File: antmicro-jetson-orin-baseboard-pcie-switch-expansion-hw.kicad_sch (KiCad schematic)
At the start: 0 parts

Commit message: [#100645] Update stackup & prepare mock
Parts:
- added A1: Mech_M2_2242_H2.5mm, antmicro-footprints:Mech_M2_2242_H2.5mm, symbol antmicroModules:Mech_M2_2242_H2.5mm
- added A2: Mech_M2_2280_H2.5mm, antmicro-footprints:Mech_M2_2280_H2.5mm, symbol antmicroModules:Mech_M2_2280_H2.5mm
- added H1, H2, H3, H4: Spacer_Drill3.7mm_H10mm_9774100151R, antmicro-footprints:Spacer_Drill3.7mm_H10mm_9774100151R, symbol antmicroMechanicalParts:Spacer_Drill3.7mm_H10mm_9774100151R
- added H5, H6, H7, H8: Spacer_Drill4.4mm_H2.5mm_9774025360R, antmicro-footprints:Spacer_Drill4.4mm_H2.5mm_9774025360R, symbol antmicroMechanicalParts:Spacer_Drill4.4mm_H2.5mm_9774025360R
- added J1, J2: Bus_M.2_1-2199230-6, antmicro-footprints:Bus_M.2_Socket_Key_M_TE_1-2199230-6, symbol antmicroPciConnectors:Bus_M.2_1-2199230-6
- added J3, J4, J5: OCuLink_x4_Amphenol_G14A421211112HR, antmicro-footprints:Amphenol_G14A421211112HR, symbol antmicroPciConnectors:OCuLink_x4_Amphenol_G14A421211112HR
- added J6: Molex_Nano-Fit_1x2_SMD_1054301202, antmicro-footprints:Conn_Molex_Nano-Fit_1x2_SMD_1054301202, symbol antmicroWire2BoardConnectors:Molex_Nano-Fit_1x2_SMD_1054301202
- added J7: Plug_Samtec_ERM8_2x40_ERM8-040-05.0-L-DV-K-TR, antmicro-footprints:Conn_Plug_Samtec_ERM8_2x40_ERM8-040-05.0-L-DV-K-TR, symbol antmicroB2BConnectors:Plug_Samtec_ERM8_2x40_ERM8-040-05.0-L-DV-K-TR
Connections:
- new net: J3.A11 (GND), J3.A14 (GND), J3.A17 (GND), J3.A2 (GND), J3.A20 (GND), J3.A5 (GND), J3.A8 (GND), J3.B11 (GND), J3.B14 (GND), J3.B17 (GND), J3.B2 (GND), J3.B20 (GND), J3.B5 (GND), J3.B8 (GND)
- new net: J3.A21 (5V), J3.B1 (5V)
- new net: J4.A11 (GND), J4.A14 (GND), J4.A17 (GND), J4.A2 (GND), J4.A20 (GND), J4.A5 (GND), J4.A8 (GND), J4.B11 (GND), J4.B14 (GND), J4.B17 (GND), J4.B2 (GND), J4.B20 (GND), J4.B5 (GND), J4.B8 (GND)
- new net: J4.A21 (5V), J4.B1 (5V)
- new net: J2.1 (GND), J2.15 (GND), J2.21 (GND), J2.27 (GND), J2.3 (GND), J2.33 (GND), J2.39 (GND), J2.45 (GND), J2.51 (GND), J2.57 (GND), J2.71 (GND), J2.73 (GND), J2.75 (GND), J2.9 (GND)
- new net: J2.12 (3V3), J2.14 (3V3), J2.16 (3V3), J2.18 (3V3), J2.2 (3V3), J2.4 (3V3), J2.70 (3V3), J2.72 (3V3), J2.74 (3V3)
- new net: J2.MP1 (MP), J2.MP2 (MP)
- new net: J1.1 (GND), J1.15 (GND), J1.21 (GND), J1.27 (GND), J1.3 (GND), J1.33 (GND), J1.39 (GND), J1.45 (GND), J1.51 (GND), J1.57 (GND), J1.71 (GND), J1.73 (GND), J1.75 (GND), J1.9 (GND)
- new net: J1.12 (3V3), J1.14 (3V3), J1.16 (3V3), J1.18 (3V3), J1.2 (3V3), J1.4 (3V3), J1.70 (3V3), J1.72 (3V3), J1.74 (3V3)
- new net: J1.MP1 (MP), J1.MP2 (MP)
- new net: J5.A11 (GND), J5.A14 (GND), J5.A17 (GND), J5.A2 (GND), J5.A20 (GND), J5.A5 (GND), J5.A8 (GND), J5.B11 (GND), J5.B14 (GND), J5.B17 (GND), J5.B2 (GND), J5.B20 (GND), J5.B5 (GND), J5.B8 (GND)
- new net: J5.A21 (5V), J5.B1 (5V)

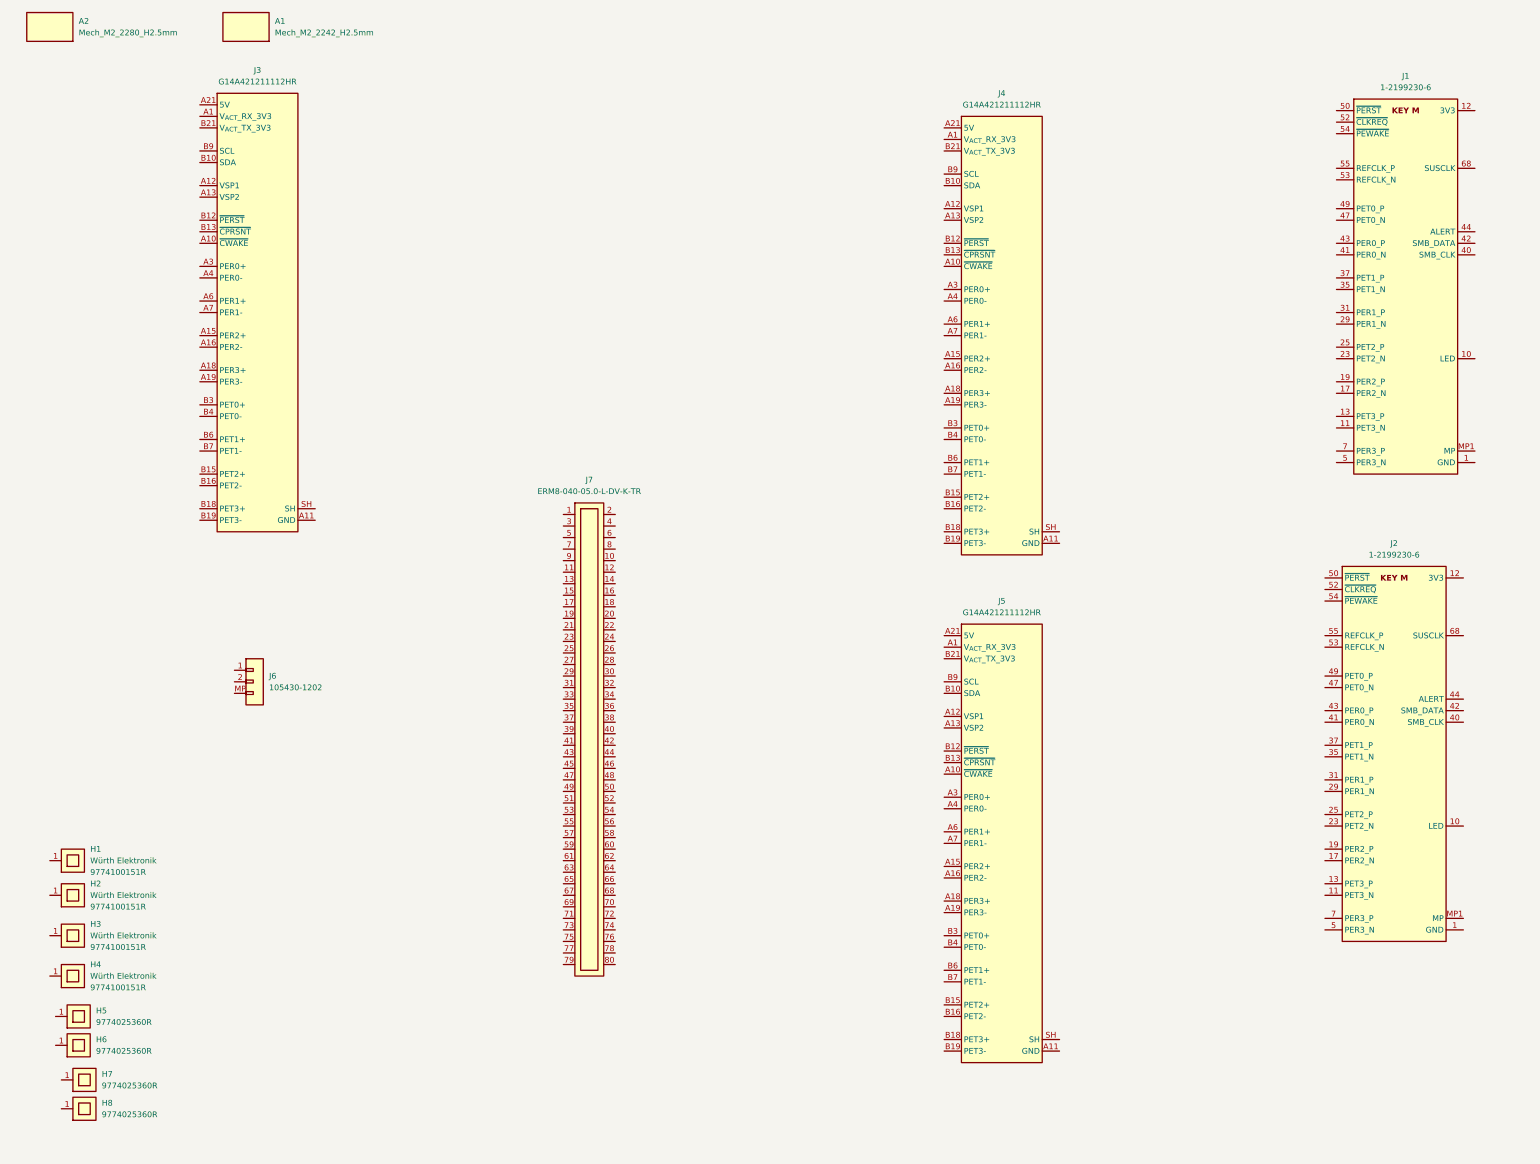
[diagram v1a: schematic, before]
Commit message: [#100765] Add subsheets, import bus alias definitions
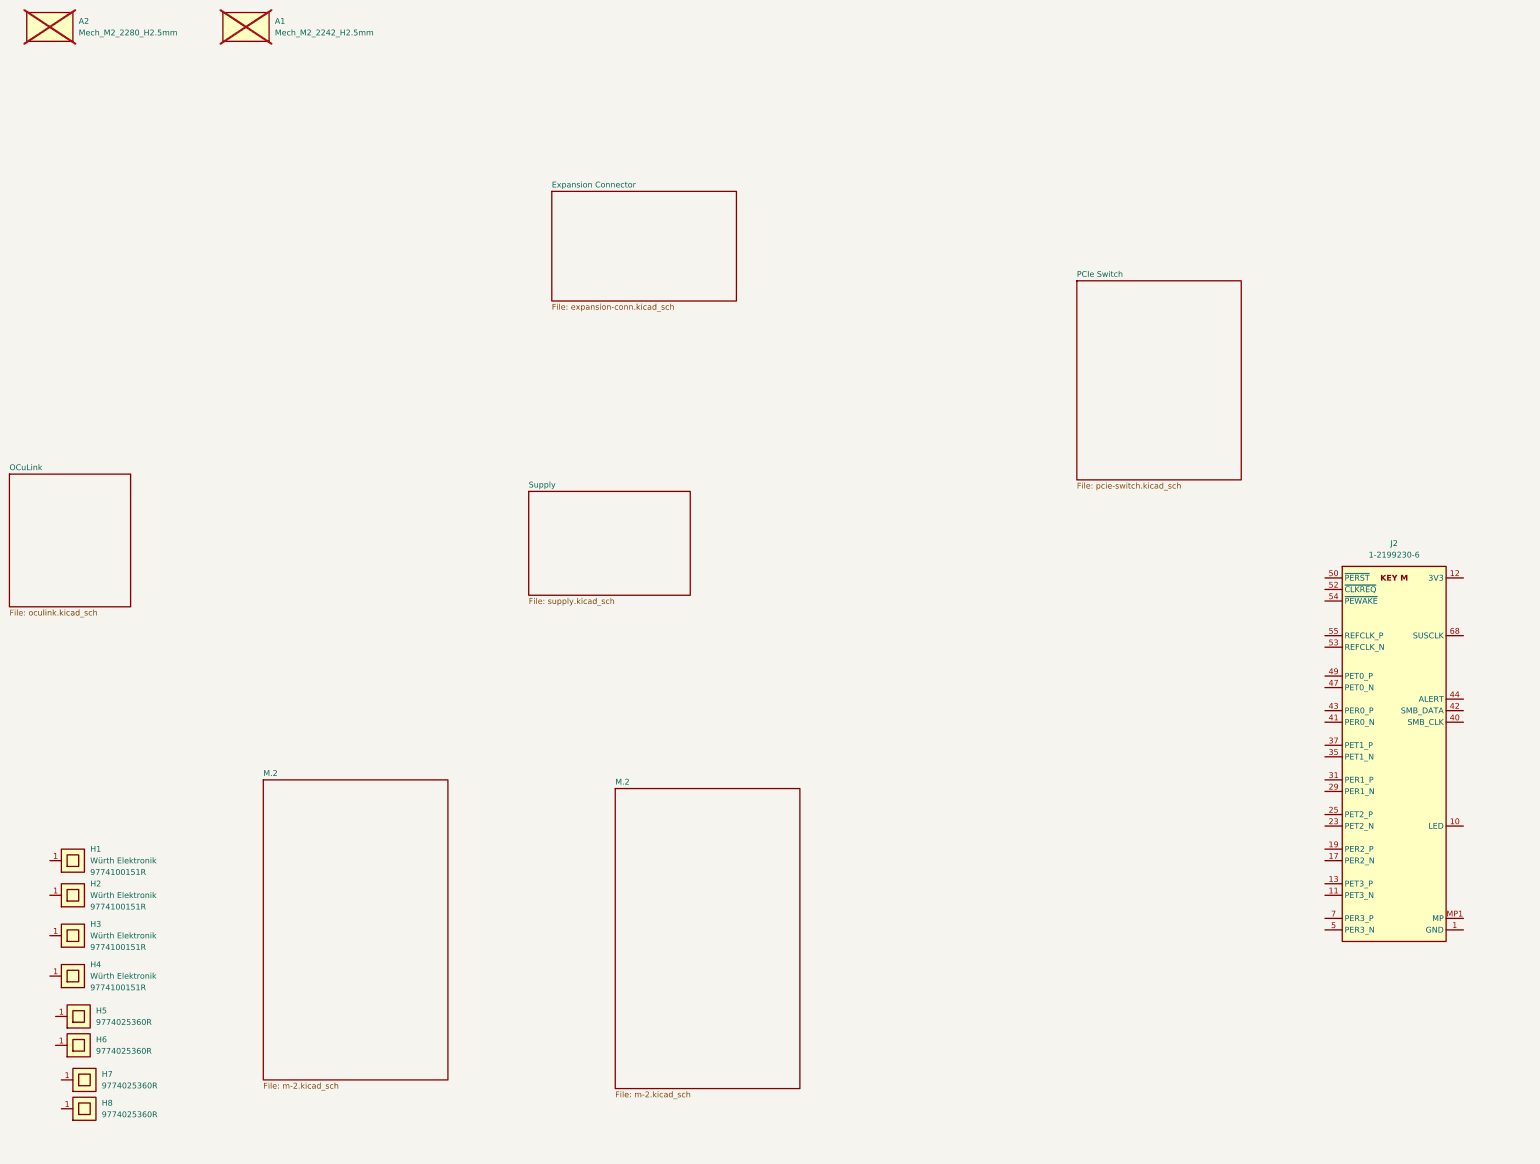
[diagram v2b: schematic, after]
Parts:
- removed J1: Bus_M.2_1-2199230-6, antmicro-footprints:Bus_M.2_Socket_Key_M_TE_1-2199230-6, symbol antmicroPciConnectors:Bus_M.2_1-2199230-6
- removed J3, J4, J5: OCuLink_x4_Amphenol_G14A421211112HR, antmicro-footprints:Amphenol_G14A421211112HR, symbol antmicroPciConnectors:OCuLink_x4_Amphenol_G14A421211112HR
- removed J6: Molex_Nano-Fit_1x2_SMD_1054301202, antmicro-footprints:Conn_Molex_Nano-Fit_1x2_SMD_1054301202, symbol antmicroWire2BoardConnectors:Molex_Nano-Fit_1x2_SMD_1054301202
- removed J7: Plug_Samtec_ERM8_2x40_ERM8-040-05.0-L-DV-K-TR, antmicro-footprints:Conn_Plug_Samtec_ERM8_2x40_ERM8-040-05.0-L-DV-K-TR, symbol antmicroB2BConnectors:Plug_Samtec_ERM8_2x40_ERM8-040-05.0-L-DV-K-TR
- A1, A2: now not fitted; now in the parts list
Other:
- added sheet Expansion Connector (expansion-conn.kicad_sch)
- added sheet M.2 (m-2.kicad_sch)
- added sheet OCuLink (oculink.kicad_sch)
- added sheet PCIe Switch (pcie-switch.kicad_sch)
- added sheet Supply (supply.kicad_sch)

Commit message: [#100765] Update Top Level schematic
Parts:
- removed J2: Bus_M.2_1-2199230-6, antmicro-footprints:Bus_M.2_Socket_Key_M_TE_1-2199230-6, symbol antmicroPciConnectors:Bus_M.2_1-2199230-6
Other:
- added sheet PCIe Mux (pcie-mux.kicad_sch)
- sheet Expansion Connector ports: added PCIe_{x2}{PCIe}, POWER_EN; removed none
- sheet M.2 ports: added PCIe_{x2}{PCIe}; removed none
- sheet OCuLink ports: added PCIe_{x2}{PCIe}; removed none
- sheet PCIe Switch ports: added PCIe_{x2_0}{PCIe}, PCIe_{x2_1}{PCIe}, PCIe_{x2}{PCIe}; removed none
- sheet Supply ports: added POWER_EN, V_{cc}; removed none

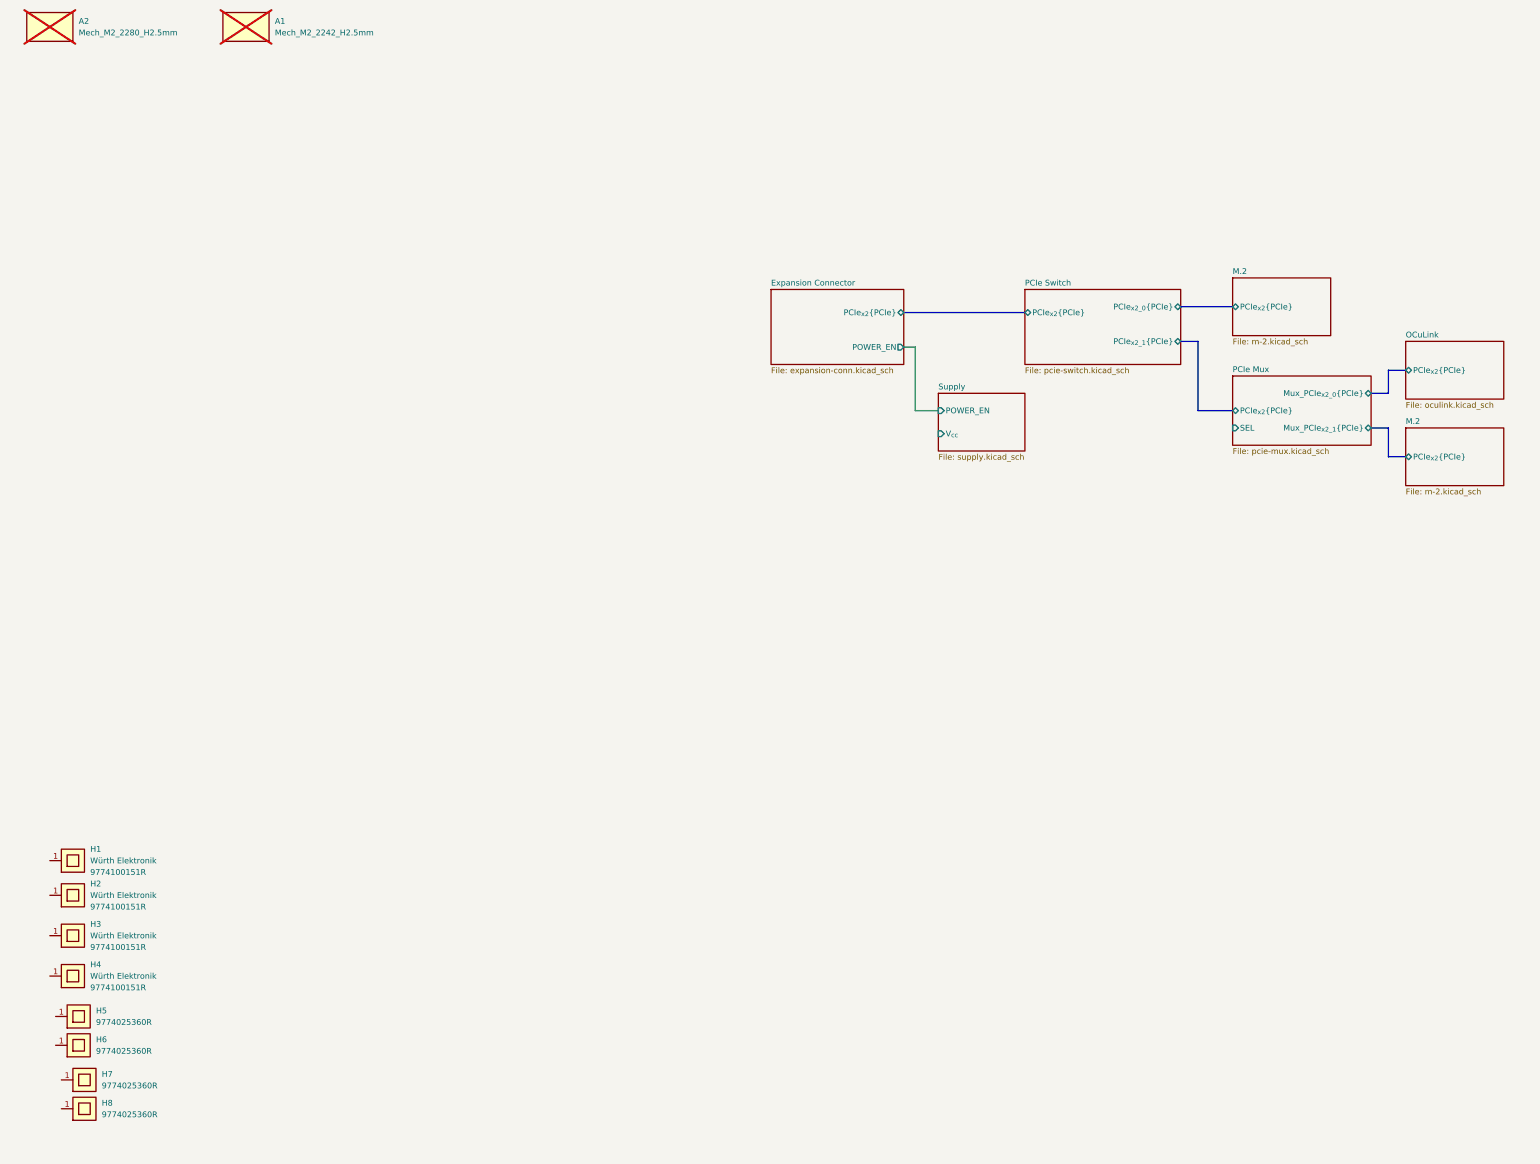
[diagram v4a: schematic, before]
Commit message: [#100765] Update top level schematic, add comments
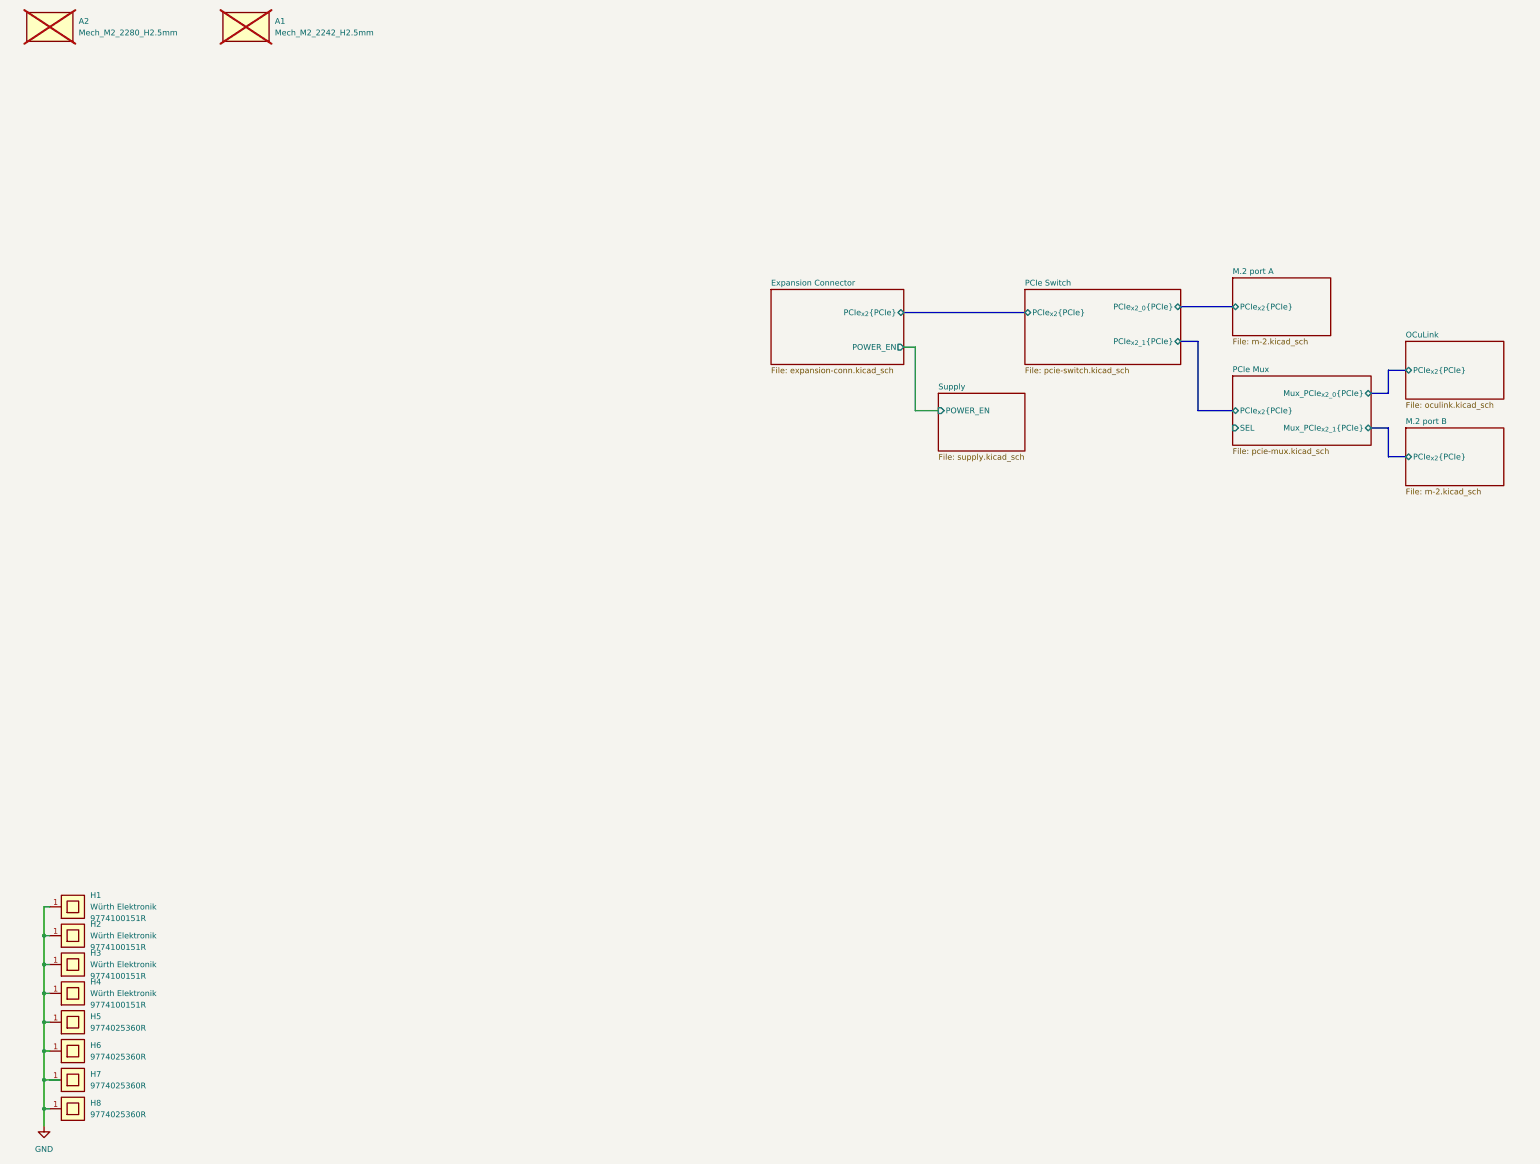
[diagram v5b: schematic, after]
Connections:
- net GND: now reaches H6.1
- net GND: now also H1.1, H2.1, H3.1, H4.1, H5.1, H7.1, H8.1
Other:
- sheet M.2 renamed M.2 port A
- added sheet M.2 port B (m-2.kicad_sch)
- sheet Supply ports: added none; removed V_{cc}
- moved on the sheet: H1, H2, H3, H4, H5, H6, H7, H8

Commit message: [#100765] Work on schematic
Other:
- added sheet Tag Connect, EEPROM (eeprom_tagconnect.kicad_sch)
- sheet PCIe Switch ports: added {I_{2}C}, {SPI}; removed none
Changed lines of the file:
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@@
 	(wire
 		(pts
-			(xy 232.41 113.03) (xy 237.49 113.03)
+			(xy 232.41 116.84) (xy 234.95 116.84)
 		)
 		(stroke
@@
 	(bus
 		(pts
+			(xy 254 97.79) (xy 256.54 97.79)
+		)
+		(stroke
+			(width 0)
+			(type default)
+		)
+	)
+	(bus
+		(pts
 			(xy 290.83 90.17) (xy 302.26 90.17)
 		)
@@
 		)
 	)
+	(bus
+		(pts
+			(xy 254 68.58) (xy 254 97.79)
+		)
+		(stroke
+			(width 0)
+			(type default)
+		)
+	)
 	(wire
 		(pts
@@
 		)
 	)
+	(bus
+		(pts
+			(xy 257.81 68.58) (xy 254 68.58)
+		)
+		(stroke
+			(width 0)
+			(type default)
+		)
+	)
 	(wire
 		(pts
-			(xy 232.41 99.06) (xy 232.41 113.03)
+			(xy 232.41 116.84) (xy 232.41 99.06)
 		)
 		(stroke
@@
 			)
 		)
+		(pin "{I_{2}C}" bidirectional
+			(at 270.51 102.87 270)
+			(effects
+				(font
+					(size 1.27 1.27)
+				)
+				(justify left)
+			)
+		)
+		(pin "{SPI}" bidirectional
+			(at 256.54 97.79 180)
+			(effects
+				(font
+					(size 1.27 1.27)
+				)
+				(justify left)
+			)
+		)
 		(instances
 			(project "antmicro-jetson-orin-baseboard-pcie-switch-expansion-hw"
@@
 	)
 	(sheet
+		(at 257.81 53.34)
+		(size 21.59 17.78)
+		(exclude_from_sim no)
+		(in_bom yes)
+		(on_board yes)
+		(dnp no)
+		(fields_autoplaced yes)
+		(stroke
+			(width 0.1524)
+			(type solid)
+		)
+		(fill
+			(color 0 0 0 0)
+		)
+		(property "Sheetname" "Tag Connect, EEPROM"
+			(at 257.81 52.6284 0)
+			(show_name no)
+			(do_not_autoplace no)
+			(effects
+				(font
+					(size 1.27 1.27)
+				)
+				(justify left bottom)
+			)
+		)
+		(property "Sheetfile" "eeprom_tagconnect.kicad_sch"
+			(at 257.81 71.7046 0)
+			(show_name no)
+			(do_not_autoplace no)
+			(effects
+				(font
+					(size 1.27 1.27)
+				)
+				(justify left top)
+			)
+		)
+		(pin "{SPI}" bidirectional
+			(at 257.81 68.58 180)
+			(effects
+				(font
+					(size 1.27 1.27)
+				)
+				(justify left)
+			)
+		)
+		(instances
+			(project "antmicro-jetson-orin-baseboard-pcie-switch-expansion-hw"
+				(path "/9f8272ef-d62d-4578-9094-a2852fcd4bf4"
+					(page "9")
+				)
+			)
+		)
+	)
+	(sheet
 		(at 302.26 105.41)
 		(size 30.48 15.24)
@@
 	)
 	(sheet
-		(at 237.49 109.22)
+		(at 234.95 113.03)
 		(size 19.05 12.7)
 		(exclude_from_sim no)
@@
 		)
 		(property "Sheetname" "Supply"
-			(at 237.49 108.5084 0)
+			(at 234.95 112.3184 0)
 			(show_name no)
 			(do_not_autoplace no)
@@
 		)
 		(property "Sheetfile" "supply.kicad_sch"
-			(at 237.49 122.5046 0)
+			(at 234.95 126.3146 0)
 			(show_name no)
 			(do_not_autoplace no)
@@
 		)
 		(pin "POWER_EN" input
-			(at 237.49 113.03 180)
-			(effects
-				(font
+			(at 234.95 116.84 180)
+			(effects
+				(font
